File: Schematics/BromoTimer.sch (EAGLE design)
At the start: 28 parts, among them IC1 PIC16F687, IC2 7805TV, K1 G2R2A, K2 G2R2A, Q1 BC548B, Q2 BC548B, Q3 BC548B, X1 AC_IN, X4 22-23-2031, X5 AC_OUT

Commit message: Component placement finished
This is just a candidate though. The area with Q1 Q2 and Q3 could get optimized
a little more though...
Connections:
- removed net N$22: TR1.P2, X1-1.KL
- net AC1: now also TR1.P2, X1-1.KL
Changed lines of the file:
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@@
 <label x="195.58" y="30.48" size="1.778" layer="95"/>
+</segment>
+<segment>
+<pinref part="X1" gate="-1" pin="KL"/>
+<pinref part="TR1" gate="1" pin="P2"/>
+<wire x1="20.32" y1="17.78" x2="33.02" y2="17.78" width="0.1524" layer="91"/>
 </segment>
 </net>
@@
 </segment>
 </net>
-<net name="N$22" class="0">
-<segment>
-<pinref part="X1" gate="-1" pin="KL"/>
-<pinref part="TR1" gate="1" pin="P2"/>
-<wire x1="20.32" y1="17.78" x2="33.02" y2="17.78" width="0.1524" layer="91"/>
-</segment>
-</net>

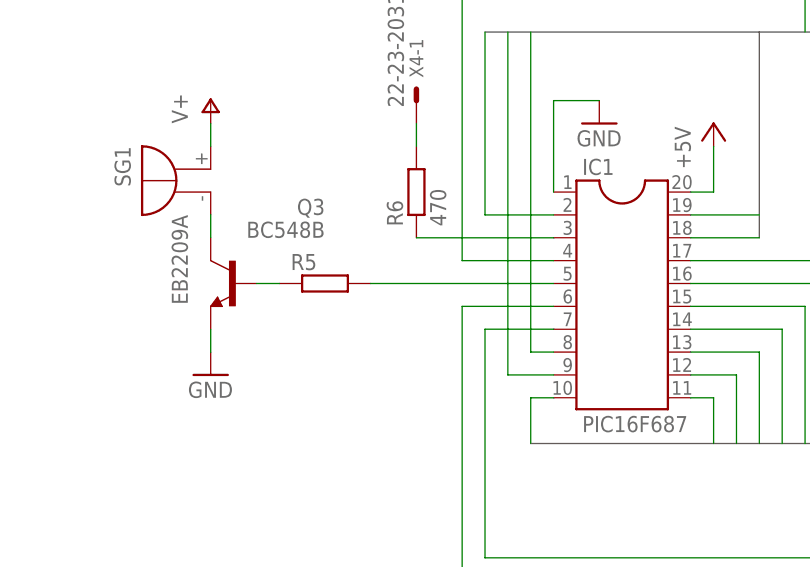
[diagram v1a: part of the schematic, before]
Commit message: Adjusted some positions in the board layout
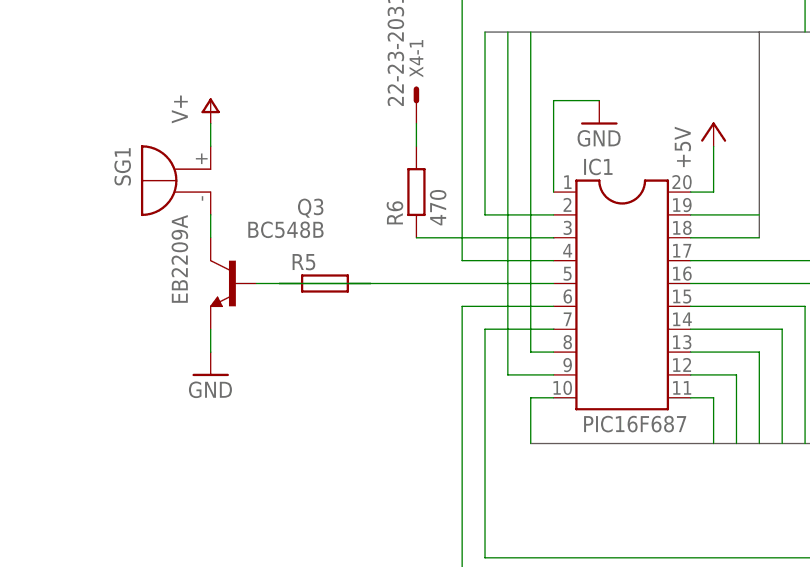
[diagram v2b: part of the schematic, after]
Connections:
- net N$17: now also R5.1; no longer R5.2
- net N$18: now also R5.2; no longer R5.1
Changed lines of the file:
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@@
 <net name="N$17" class="0">
 <segment>
-<pinref part="R5" gate="G$1" pin="2"/>
+<pinref part="R5" gate="G$1" pin="1"/>
 <pinref part="IC1" gate="G$1" pin="5"/>
-<wire x1="86.36" y1="116.84" x2="106.68" y2="116.84" width="0.1524" layer="91"/>
+<wire x1="76.2" y1="116.84" x2="106.68" y2="116.84" width="0.1524" layer="91"/>
 </segment>
 </net>
@@
 <segment>
 <pinref part="Q3" gate="G$1" pin="B"/>
-<pinref part="R5" gate="G$1" pin="1"/>
-<wire x1="73.66" y1="116.84" x2="76.2" y2="116.84" width="0.1524" layer="91"/>
+<pinref part="R5" gate="G$1" pin="2"/>
+<wire x1="73.66" y1="116.84" x2="86.36" y2="116.84" width="0.1524" layer="91"/>
 </segment>
 </net>

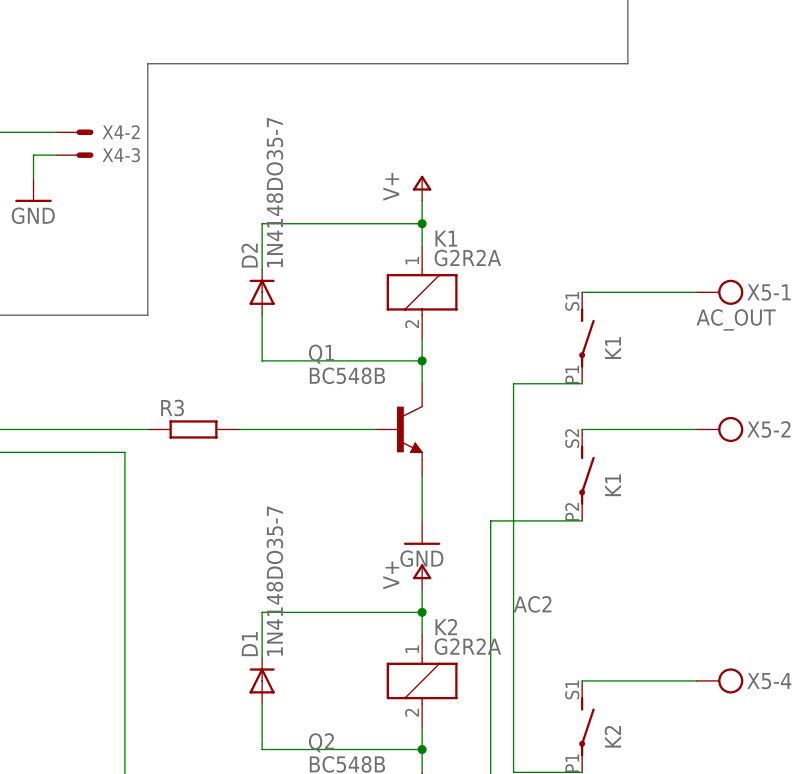
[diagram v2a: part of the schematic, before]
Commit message: Relay coil voltage is 5V
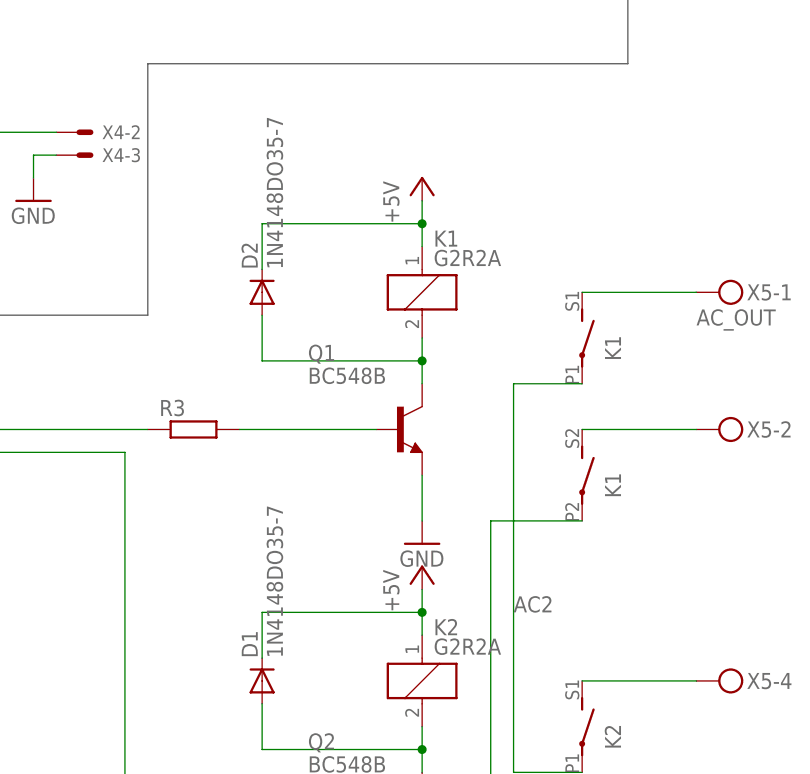
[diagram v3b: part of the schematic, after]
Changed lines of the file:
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@@
 <part name="P+8" library="supply1" deviceset="V+" device=""/>
 <part name="GND8" library="supply1" deviceset="GND" device=""/>
-<part name="P+5" library="supply1" deviceset="V+" device=""/>
-<part name="P+6" library="supply1" deviceset="V+" device=""/>
+<part name="P+5" library="supply1" deviceset="+5V" device=""/>
+<part name="P+6" library="supply1" deviceset="+5V" device=""/>
 <part name="D1" library="diode" deviceset="1N4148" device="DO35-7"/>
 <part name="D2" library="diode" deviceset="1N4148" device="DO35-7"/>
@@
 <pinref part="K2" gate="1" pin="1"/>
 <wire x1="187.96" y1="68.58" x2="187.96" y2="66.04" width="0.1524" layer="91"/>
-<pinref part="P+5" gate="1" pin="V+"/>
+<pinref part="P+5" gate="1" pin="+5V"/>
 <pinref part="D1" gate="G$1" pin="C"/>
 <wire x1="187.96" y1="66.04" x2="187.96" y2="63.5" width="0.1524" layer="91"/>
@@
 <pinref part="K1" gate="1" pin="1"/>
 <wire x1="187.96" y1="111.76" x2="187.96" y2="109.22" width="0.1524" layer="91"/>
-<pinref part="P+6" gate="1" pin="V+"/>
+<pinref part="P+6" gate="1" pin="+5V"/>
 <pinref part="D2" gate="G$1" pin="C"/>
 <wire x1="187.96" y1="109.22" x2="187.96" y2="106.68" width="0.1524" layer="91"/>

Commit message: Routing nearly done
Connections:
- net +5V: now also D1.C, D2.C, K11.1, K21.1
- net V+: no longer D1.C, D2.C, K11.1, K21.1
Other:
- moved on the sheet: R5
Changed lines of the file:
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@@
 <instance part="D3" gate="1" x="40.64" y="71.12" rot="R180"/>
 <instance part="Q3" gate="G$1" x="71.12" y="116.84" rot="MR0"/>
-<instance part="R5" gate="G$1" x="81.28" y="116.84"/>
+<instance part="R5" gate="G$1" x="81.28" y="116.84" rot="R180"/>
 <instance part="GND11" gate="1" x="68.58" y="106.68"/>
 <instance part="P+10" gate="1" x="68.58" y="137.16"/>
@@
 <junction x="55.88" y="71.12"/>
 </segment>
+<segment>
+<pinref part="K2" gate="1" pin="1"/>
+<wire x1="187.96" y1="68.58" x2="187.96" y2="66.04" width="0.1524" layer="91"/>
+<pinref part="P+5" gate="1" pin="+5V"/>
+<pinref part="D1" gate="G$1" pin="C"/>
+<wire x1="187.96" y1="66.04" x2="187.96" y2="63.5" width="0.1524" layer="91"/>
+<wire x1="170.18" y1="60.96" x2="170.18" y2="66.04" width="0.1524" layer="91"/>
+<wire x1="170.18" y1="66.04" x2="187.96" y2="66.04" width="0.1524" layer="91"/>
+<junction x="187.96" y="66.04"/>
+</segment>
+<segment>
+<pinref part="K1" gate="1" pin="1"/>
+<wire x1="187.96" y1="111.76" x2="187.96" y2="109.22" width="0.1524" layer="91"/>
+<pinref part="P+6" gate="1" pin="+5V"/>
+<pinref part="D2" gate="G$1" pin="C"/>
+<wire x1="187.96" y1="109.22" x2="187.96" y2="106.68" width="0.1524" layer="91"/>
+<wire x1="170.18" y1="104.14" x2="170.18" y2="109.22" width="0.1524" layer="91"/>
+<wire x1="170.18" y1="109.22" x2="187.96" y2="109.22" width="0.1524" layer="91"/>
+<junction x="187.96" y="109.22"/>
+</segment>
 </net>
 <net name="GND" class="0">
@@
 <segment>
 <wire x1="22.86" y1="30.48" x2="33.02" y2="30.48" width="0.1524" layer="91"/>
-<label x="25.4" y="33.02" size="1.778" layer="94"/>
+<label x="25.4" y="30.48" size="1.778" layer="95"/>
 <pinref part="TR1" gate="1" pin="P1"/>
 <pinref part="X1" gate="-3" pin="KL"/>
@@
 <pinref part="TR1" gate="1" pin="P2"/>
 <wire x1="20.32" y1="17.78" x2="33.02" y2="17.78" width="0.1524" layer="91"/>
+<label x="25.4" y="15.24" size="1.778" layer="95"/>
 </segment>
 </net>
@@
 </segment>
 <segment>
-<pinref part="K2" gate="1" pin="1"/>
-<wire x1="187.96" y1="68.58" x2="187.96" y2="66.04" width="0.1524" layer="91"/>
-<pinref part="P+5" gate="1" pin="+5V"/>
-<pinref part="D1" gate="G$1" pin="C"/>
-<wire x1="187.96" y1="66.04" x2="187.96" y2="63.5" width="0.1524" layer="91"/>
-<wire x1="170.18" y1="60.96" x2="170.18" y2="66.04" width="0.1524" layer="91"/>
-<wire x1="170.18" y1="66.04" x2="187.96" y2="66.04" width="0.1524" layer="91"/>
-<junction x="187.96" y="66.04"/>
-</segment>
-<segment>
-<pinref part="K1" gate="1" pin="1"/>
-<wire x1="187.96" y1="111.76" x2="187.96" y2="109.22" width="0.1524" layer="91"/>
-<pinref part="P+6" gate="1" pin="+5V"/>
-<pinref part="D2" gate="G$1" pin="C"/>
-<wire x1="187.96" y1="109.22" x2="187.96" y2="106.68" width="0.1524" layer="91"/>
-<wire x1="170.18" y1="104.14" x2="170.18" y2="109.22" width="0.1524" layer="91"/>
-<wire x1="170.18" y1="109.22" x2="187.96" y2="109.22" width="0.1524" layer="91"/>
-<junction x="187.96" y="109.22"/>
-</segment>
-<segment>
 <pinref part="P+10" gate="1" pin="V+"/>
 <wire x1="68.58" y1="134.62" x2="68.58" y2="132.08" width="0.1524" layer="91"/>
@@
 <pinref part="R5" gate="G$1" pin="1"/>
 <pinref part="IC1" gate="G$1" pin="5"/>
-<wire x1="76.2" y1="116.84" x2="106.68" y2="116.84" width="0.1524" layer="91"/>
+<wire x1="86.36" y1="116.84" x2="106.68" y2="116.84" width="0.1524" layer="91"/>
 </segment>
 </net>
@@
 <pinref part="Q3" gate="G$1" pin="B"/>
 <pinref part="R5" gate="G$1" pin="2"/>
-<wire x1="73.66" y1="116.84" x2="86.36" y2="116.84" width="0.1524" layer="91"/>
-</segment>
-</net>
+<wire x1="73.66" y1="116.84" x2="76.2" y2="116.84" width="0.1524" layer="91"/>
+</segment>
+</net>

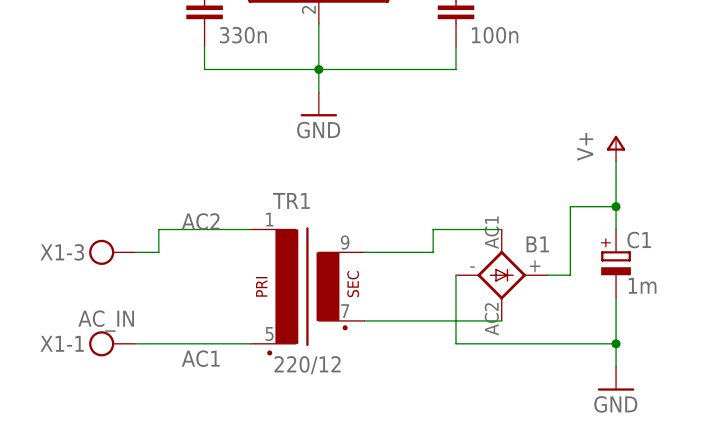
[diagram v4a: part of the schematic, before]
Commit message: Integrating a fuse in the circuit
Moved the supply circuit a bit to make room for the fuse holder.
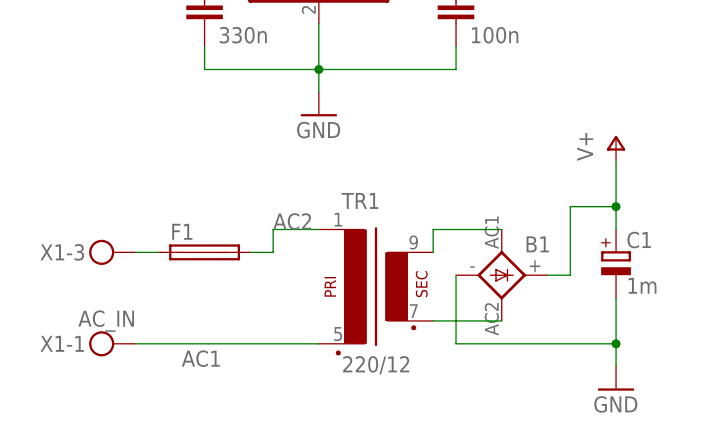
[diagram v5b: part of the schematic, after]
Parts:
- added F1: (no value), fuse:GSH15
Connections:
- new net N$22: F1.1, X1-3.KL
- net AC2: now also F1.2; no longer X1-3.KL
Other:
- moved on the sheet: TR1
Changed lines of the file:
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@@
 <part name="X1" library="con-phoenix-508" deviceset="MKDSN1,5/3-5,08" device="" value="AC_IN"/>
 <part name="X5" library="con-phoenix-508" deviceset="MKDSN1,5/5-5,08" device="" value="AC_OUT"/>
+<part name="F1" library="fuse" deviceset="GSH15" device=""/>
 </parts>
 <sheets>
@@
 <instance part="GND9" gate="1" x="144.78" y="111.76"/>
 <instance part="SG1" gate="G$1" x="66.04" y="129.54" rot="MR270"/>
-<instance part="TR1" gate="1" x="38.1" y="25.4"/>
+<instance part="TR1" gate="1" x="45.72" y="25.4"/>
 <instance part="C3" gate="G$1" x="27.94" y="55.88"/>
 <instance part="R6" gate="G$1" x="91.44" y="127" rot="R90"/>
@@
 <instance part="X5" gate="-4" x="220.98" y="58.42"/>
 <instance part="X5" gate="-5" x="220.98" y="43.18"/>
+<instance part="F1" gate="1" x="27.94" y="27.94"/>
 </instances>
 <busses>
@@
 </segment>
 <segment>
-<wire x1="22.86" y1="30.48" x2="33.02" y2="30.48" width="0.1524" layer="91"/>
-<label x="25.4" y="30.48" size="1.778" layer="95"/>
+<wire x1="35.56" y1="30.48" x2="40.64" y2="30.48" width="0.1524" layer="91"/>
+<label x="35.56" y="30.48" size="1.778" layer="95"/>
 <pinref part="TR1" gate="1" pin="P1"/>
-<pinref part="X1" gate="-3" pin="KL"/>
-<wire x1="22.86" y1="30.48" x2="22.86" y2="27.94" width="0.1524" layer="91"/>
-<wire x1="22.86" y1="27.94" x2="20.32" y2="27.94" width="0.1524" layer="91"/>
+<pinref part="F1" gate="1" pin="2"/>
+<wire x1="33.02" y1="27.94" x2="35.56" y2="27.94" width="0.1524" layer="91"/>
+<wire x1="35.56" y1="27.94" x2="35.56" y2="30.48" width="0.1524" layer="91"/>
 </segment>
 </net>
@@
 <pinref part="X1" gate="-1" pin="KL"/>
 <pinref part="TR1" gate="1" pin="P2"/>
-<wire x1="20.32" y1="17.78" x2="33.02" y2="17.78" width="0.1524" layer="91"/>
+<wire x1="20.32" y1="17.78" x2="40.64" y2="17.78" width="0.1524" layer="91"/>
 <label x="25.4" y="15.24" size="1.778" layer="95"/>
 </segment>
@@
 <wire x1="53.34" y1="30.48" x2="53.34" y2="27.94" width="0.1524" layer="91"/>
 <pinref part="TR1" gate="1" pin="S4"/>
-<wire x1="53.34" y1="27.94" x2="45.72" y2="27.94" width="0.1524" layer="91"/>
 </segment>
 </net>
@@
 <pinref part="B1" gate="1" pin="AC2"/>
 <pinref part="TR1" gate="1" pin="S3"/>
-<wire x1="60.96" y1="20.32" x2="45.72" y2="20.32" width="0.1524" layer="91"/>
-</segment>
-</net>
+<wire x1="60.96" y1="20.32" x2="53.34" y2="20.32" width="0.1524" layer="91"/>
+</segment>
+</net>
+<net name="N$22" class="0">
+<segment>
+<pinref part="X1" gate="-3" pin="KL"/>
+<pinref part="F1" gate="1" pin="1"/>
+<wire x1="20.32" y1="27.94" x2="22.86" y2="27.94" width="0.1524" layer="91"/>
+</segment>
+</net>

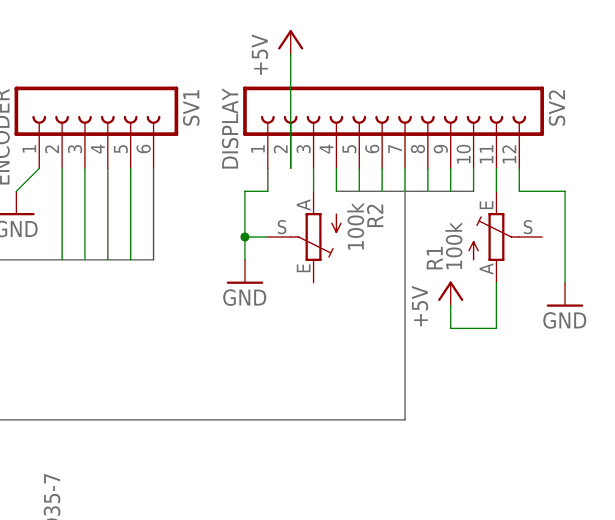
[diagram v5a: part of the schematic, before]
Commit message: Routing completed, no jumper wires
Routing fully completed, RDC passing.
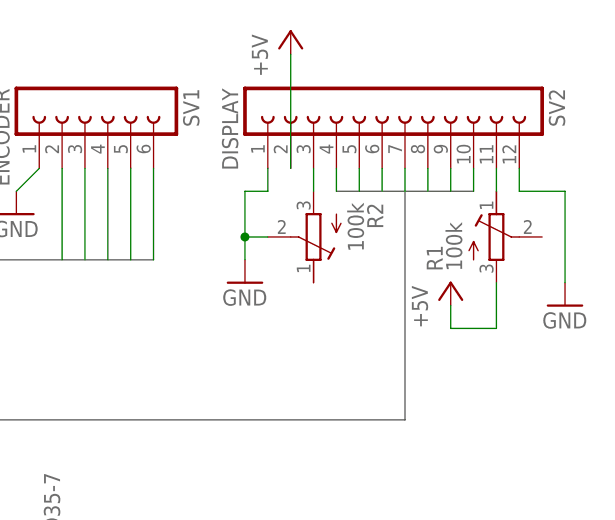
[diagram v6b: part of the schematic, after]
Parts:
- F1: device fuse:GSH15 -> fuse:SH22; OC_FARNELL (none) -> unknown; OC_NEWARK (none) -> unknown
- R1, R2: device pot:TRIM_EU-B25V -> rcl:R-TRIMMT93YB
- TR1: device trafo:EI38-1 -> trafo:EI30-1
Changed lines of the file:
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@@
 <part name="GND4" library="supply1" deviceset="GND" device=""/>
 <part name="P+3" library="supply1" deviceset="+5V" device=""/>
-<part name="R1" library="pot" deviceset="TRIM_EU-" device="B25V" value="100k"/>
-<part name="R2" library="pot" deviceset="TRIM_EU-" device="B25V" value="100k"/>
+<part name="R1" library="rcl" deviceset="R-TRIMM" device="T93YB" value="100k"/>
+<part name="R2" library="rcl" deviceset="R-TRIMM" device="T93YB" value="100k"/>
 <part name="P+4" library="supply1" deviceset="+5V" device=""/>
 <part name="Q1" library="transistor-npn" deviceset="BC548*" device="" technology="B" value="BC548B"/>
@@
 <part name="GND9" library="supply1" deviceset="GND" device=""/>
 <part name="SG1" library="buzzer" deviceset="EB2209A" device=""/>
-<part name="TR1" library="trafo" deviceset="EI38-1" device="" value="220/12"/>
+<part name="TR1" library="trafo" deviceset="EI30-1" device="" value="220/12"/>
 <part name="C3" library="rcl" deviceset="C-EU" device="050-050X075" value="330n"/>
 <part name="R6" library="rcl" deviceset="R-EU_" device="0207/10" value="470"/>
 <part name="X1" library="con-phoenix-508" deviceset="MKDSN1,5/3-5,08" device="" value="AC_IN"/>
 <part name="X5" library="con-phoenix-508" deviceset="MKDSN1,5/5-5,08" device="" value="AC_OUT"/>
-<part name="F1" library="fuse" deviceset="GSH15" device=""/>
+<part name="F1" library="fuse" deviceset="SH22" device="">
+<attribute name="MPN" value=""/>
+<attribute name="OC_FARNELL" value="unknown"/>
+<attribute name="OC_NEWARK" value="unknown"/>
+</part>
 </parts>
 <sheets>
@@
 <instance part="GND4" gate="1" x="228.6" y="139.7"/>
 <instance part="P+3" gate="1" x="198.12" y="170.18"/>
-<instance part="R1" gate="1" x="220.98" y="147.32"/>
-<instance part="R2" gate="1" x="200.66" y="147.32" rot="R180"/>
+<instance part="R1" gate="G$1" x="220.98" y="147.32"/>
+<instance part="R2" gate="G$1" x="200.66" y="147.32" rot="R180"/>
 <instance part="P+4" gate="1" x="215.9" y="142.24"/>
 <instance part="Q1" gate="G$1" x="185.42" y="86.36"/>
@@
 <pinref part="P+4" gate="1" pin="+5V"/>
 <wire x1="215.9" y1="139.7" x2="215.9" y2="137.16" width="0.1524" layer="91"/>
-<pinref part="R1" gate="1" pin="A"/>
+<pinref part="R1" gate="G$1" pin="A"/>
 <wire x1="215.9" y1="137.16" x2="220.98" y2="137.16" width="0.1524" layer="91"/>
 <wire x1="220.98" y1="137.16" x2="220.98" y2="142.24" width="0.1524" layer="91"/>
@@
 <wire x1="195.58" y1="152.4" x2="193.04" y2="152.4" width="0.1524" layer="91"/>
 <wire x1="193.04" y1="152.4" x2="193.04" y2="147.32" width="0.1524" layer="91"/>
-<pinref part="R2" gate="1" pin="S"/>
+<pinref part="R2" gate="G$1" pin="S"/>
 <wire x1="193.04" y1="147.32" x2="193.04" y2="144.78" width="0.1524" layer="91"/>
 <wire x1="195.58" y1="147.32" x2="193.04" y2="147.32" width="0.1524" layer="91"/>
@@
 <pinref part="SV2" gate="G$1" pin="11"/>
 <wire x1="220.98" y1="154.94" x2="220.98" y2="152.4" width="0.1524" layer="91"/>
-<pinref part="R1" gate="1" pin="E"/>
+<pinref part="R1" gate="G$1" pin="E"/>
 </segment>
 </net>
@@
 <segment>
 <pinref part="SV2" gate="G$1" pin="3"/>
-<pinref part="R2" gate="1" pin="A"/>
+<pinref part="R2" gate="G$1" pin="A"/>
 <wire x1="200.66" y1="154.94" x2="200.66" y2="152.4" width="0.1524" layer="91"/>
 </segment>
